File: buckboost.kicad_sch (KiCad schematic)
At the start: 22 parts, among them Q1 30V/20A_NFET, Q2 30V/20A_NFET, Q3 30V/20A_NFET, Q4 30V/20A_NFET, U1 LM5176PWP

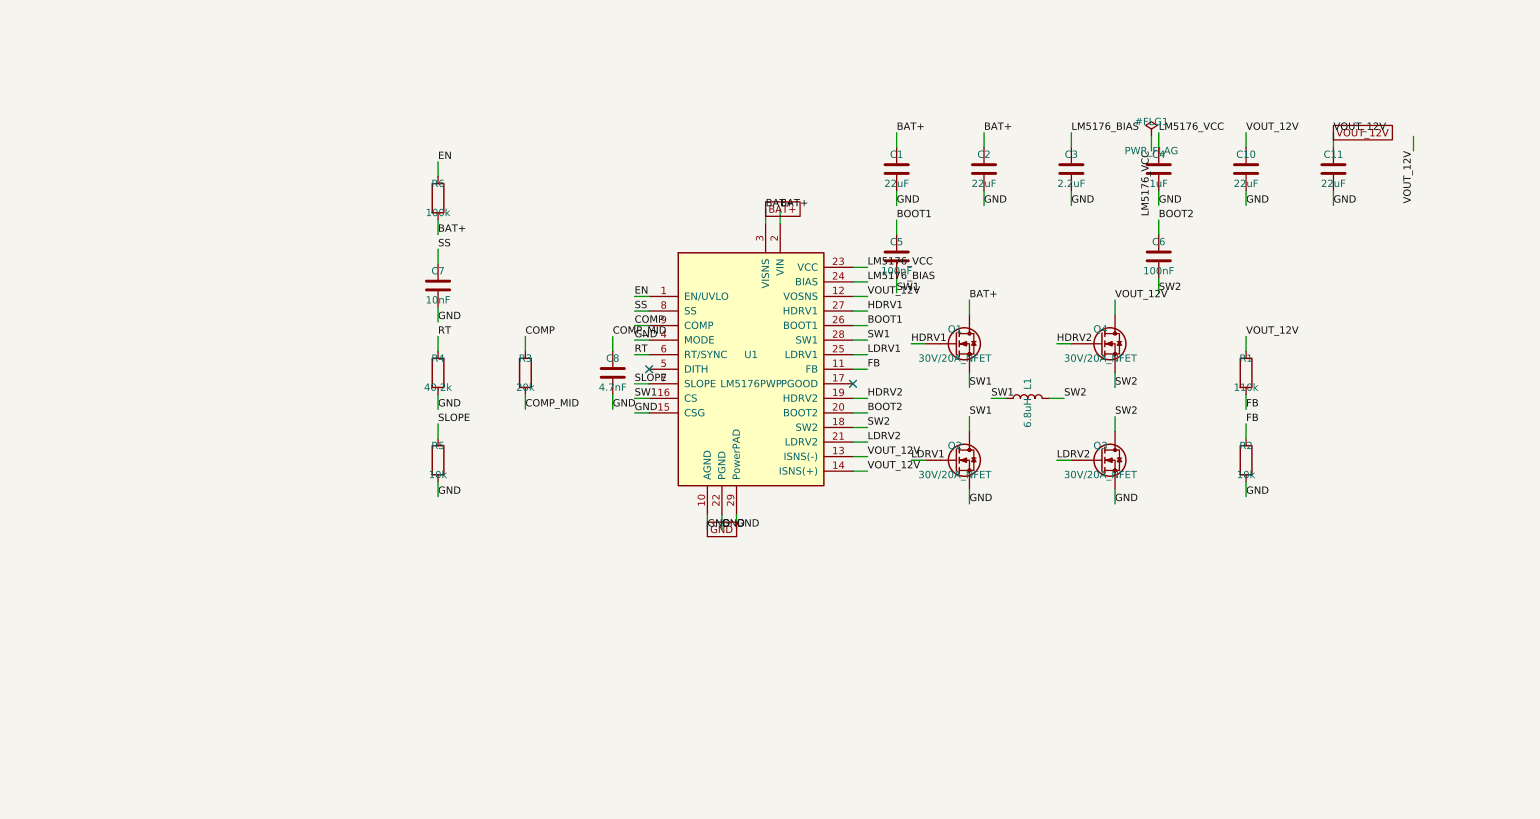
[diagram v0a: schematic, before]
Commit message: sheets: autoplace + rewire all four with default recipe
Ran PLACER.recipe(target) (shipped defaults — cluster→spread→polarize→
settle, peak repulsion ≈ 51.2) followed by apply(rewire=True) on each
sub-sheet. rewire_session's connect_pins(style="auto") replaces the
per-pin label stubs with routed wires wherever the router can find a
clear path — so this commit closes both #63 (autoplace) and the label→
wire portion of #64 in one pass.

Result: real routed wires visible on every sheet instead of the sea
of per-pin labels the hand-laid grid had. Sheets are ~1.4-2× wider
than the tight hand grid (110×56 → 230×138 on charger, similar on
buckboost) but the tradeoff is intended — visible traces make the
schematic actually readable.

ERC after commit: 0 errors, 34 cosmetic warnings (Unspecified/Passive
pin-type quirks + intentional local↔global label pairs).

Recent MCP-server fixes that made this pass work end-to-end:
  ed1f8e2 — global_labels restored after rewire (BAT+/GND/VBUS_9V)
  54d788f — pin_world unrounded so FET-gate coords don't drop
  7572032 — hierarchical instances path emitted correctly

Snapshots of the hand-laid state at
/tmp/claude-1000/{bms,charger,input,buckboost}.hand.kicad_sch for
comparison / rollback.

Co-Authored-By: Claude Opus 4.7 <noreply@anthropic.com>
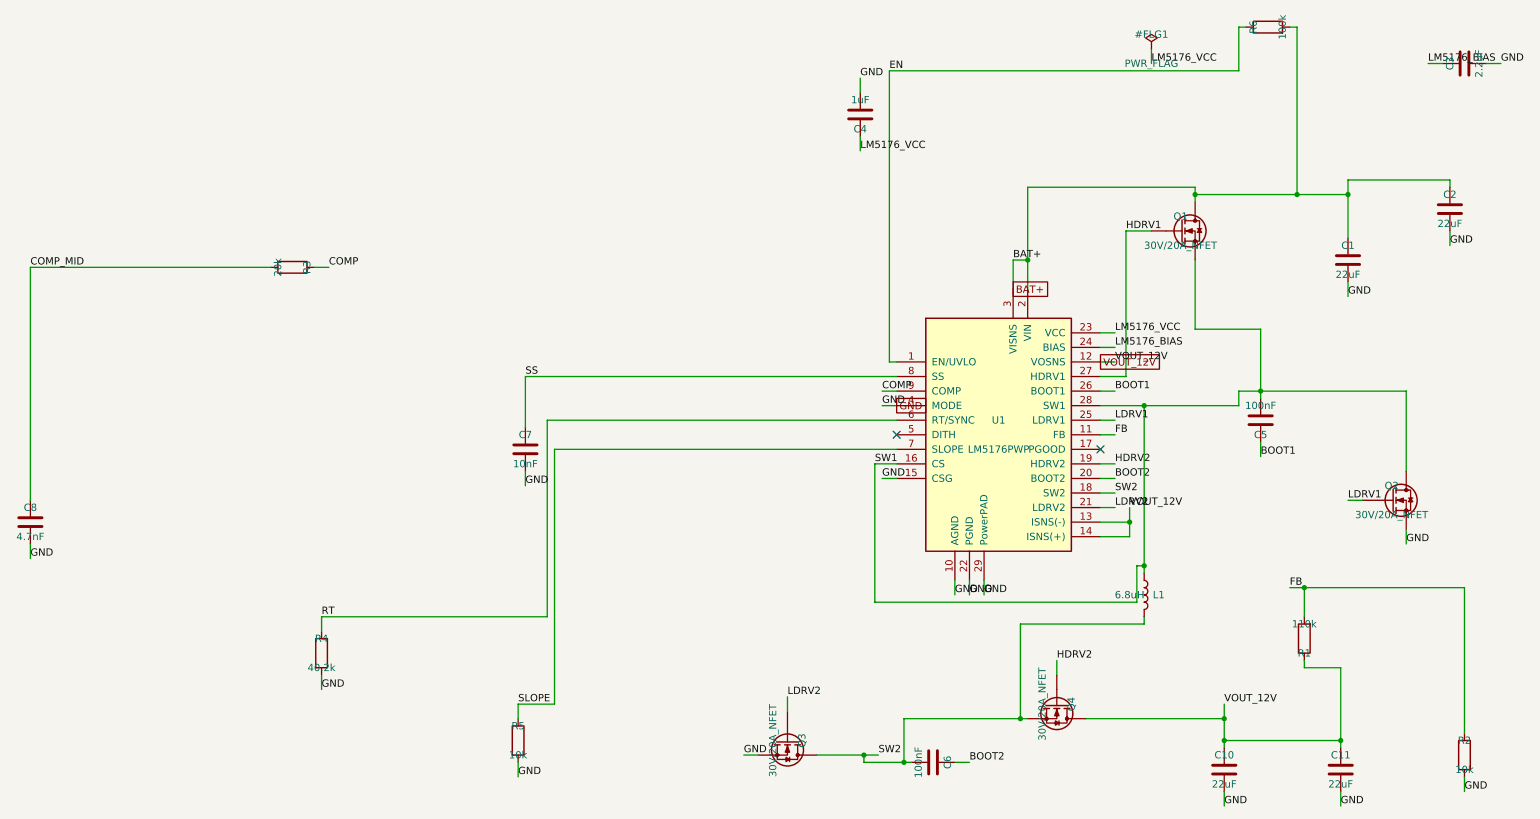
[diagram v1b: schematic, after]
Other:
- moved on the sheet: C1, C10, C11, C2, C3, C4, C5, C6, C7, C8, L1, Q1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
